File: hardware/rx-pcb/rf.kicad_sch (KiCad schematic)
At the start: 1 part

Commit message: minor board updates. added the MLPF-WB chip for stm impedance matching
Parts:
- removed FL1: MLPF-WB-01D3, easyeda2kicad:BGA-6_L1.6-W1.0-R3-C2-P0.50-TL, symbol easyeda2kicad:MLPF-WB-01D3
- added FL1: MLPF-WB-01D3, easyeda:BGA-6_L1.6-W1.0-R3-C2-P0.50-TL, symbol easyeda:MLPF-WB-01D3
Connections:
- net GND: now also FL1.A2 (GND4), FL1.B1 (GND3), FL1.B2 (GND2), FL1.B3 (GND1)
- net RF1: now also FL1.A3 (IN)
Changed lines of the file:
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@@
 		(instances
 			(project "rx-pcb"
-				(path "/9df8ddb8-545e-44cf-b4e7-941b19ec42ab/84ed0e1d-ea4c-4524-b4ef-48cf817ee110"
-					(reference "#PWR017")
-					(unit 1)
-				)
 				(path "/9df8ddb8-545e-44cf-b4e7-941b19ec42ab/f451fa07-6b2e-4005-ab57-ecfade312cca"
 					(reference "#PWR016")
@@
 	)
 	(symbol
-		(lib_id "easyeda2kicad:MLPF-WB-01D3")
+		(lib_id "easyeda:MLPF-WB-01D3")
 		(at 48.26 62.23 270)
 		(unit 1)
@@
 			)
 		)
-		(property "Footprint" "easyeda2kicad:BGA-6_L1.6-W1.0-R3-C2-P0.50-TL"
+		(property "Footprint" "easyeda:BGA-6_L1.6-W1.0-R3-C2-P0.50-TL"
 			(at 38.1 62.23 0)
 			(effects
@@
 			)
 		)
-		(property "Datasheet" ""
-			(at 48.26 62.23 0)
+		(property "Datasheet" "https://www.lcsc.com/datasheet/C5440144.pdf"
+			(at 35.56 62.23 0)
 			(effects
 				(font
@@
 			)
 		)
+		(property "Manufacturer" "ST(意法半导体)"
+			(at 33.02 62.23 0)
+			(effects
+				(font
+					(size 1.27 1.27)
+				)
+				(hide yes)
+			)
+		)
+		(property "MPN" "MLPF-WB-01D3"
+			(at 30.48 62.23 0)
+			(effects
+				(font
+					(size 1.27 1.27)
+				)
+				(hide yes)
+			)
+		)
 		(property "LCSC Part" "C5440144"
-			(at 35.56 62.23 0)
+			(at 27.94 62.23 0)
 			(effects
 				(font
@@
 		(pin "A1"
 		)
-		(pin "A2"
+		(pin "B2"
 		)
 		(pin "B1"
 		)
-		(pin "B2"
-		)
 		(pin "B3"
 		)
+		(pin "A2"
+		)
 		(instances
-			(project ""
-				(path "/9df8ddb8-545e-44cf-b4e7-941b19ec42ab/84ed0e1d-ea4c-4524-b4ef-48cf817ee110"
-					(reference "FL2")
-					(unit 1)
-				)
+			(project "rx-pcb"
 				(path "/9df8ddb8-545e-44cf-b4e7-941b19ec42ab/f451fa07-6b2e-4005-ab57-ecfade312cca"
 					(reference "FL1")
@@
 		)
 		(instances
-			(project ""
-				(path "/9df8ddb8-545e-44cf-b4e7-941b19ec42ab/84ed0e1d-ea4c-4524-b4ef-48cf817ee110"
-					(reference "#PWR015")
-					(unit 1)
-				)
+			(project "rx-pcb"
 				(path "/9df8ddb8-545e-44cf-b4e7-941b19ec42ab/f451fa07-6b2e-4005-ab57-ecfade312cca"
 					(reference "#PWR06")

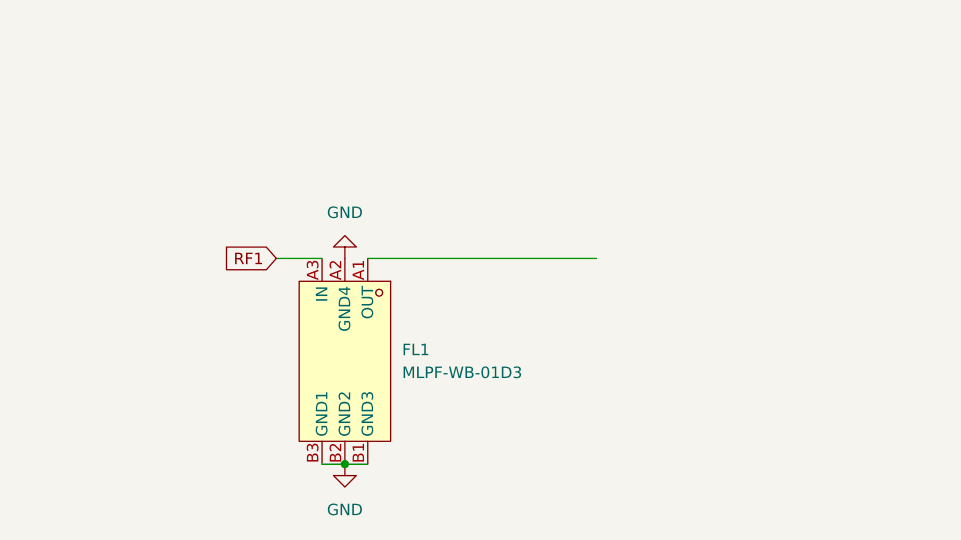
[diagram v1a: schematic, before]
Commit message: finished initial board. no sensors or power harvesting, but its programmable and bluetooth should work.
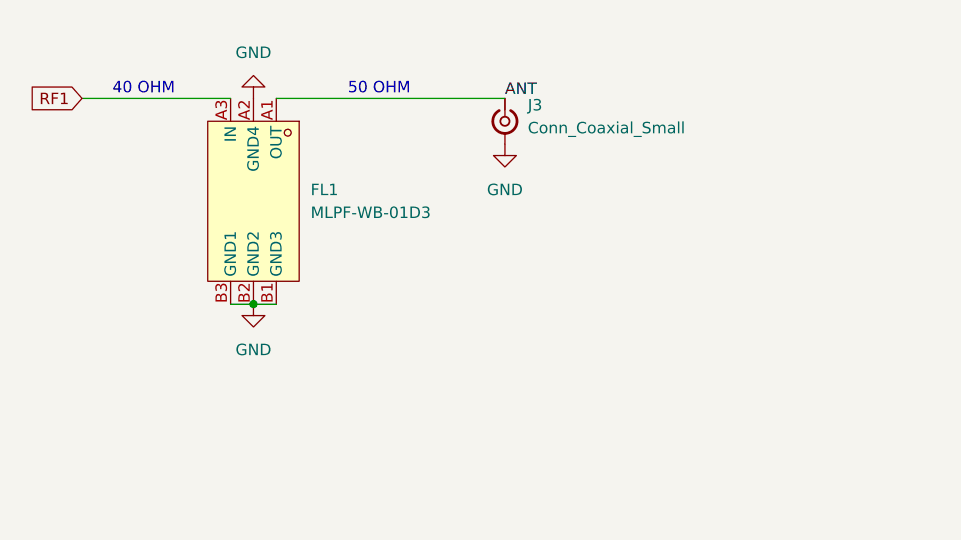
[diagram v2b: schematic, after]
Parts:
- removed FL1: MLPF-WB-01D3, easyeda:BGA-6_L1.6-W1.0-R3-C2-P0.50-TL, symbol easyeda:MLPF-WB-01D3
- added FL1: MLPF-WB-01D3, rx-parts:BGA-6_L1.6-W1.0-R3-C2-P0.50-TL, symbol rx-parts:MLPF-WB-01D3
- added J3: Conn_Coaxial_Small, rx-parts:SMA_Amphenol_901-143_Horizontal, symbol rx-parts:Conn_Coaxial_Small
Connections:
- net GND: now also FL1.A2 (GND4), FL1.B1 (GND3), FL1.B2 (GND2), FL1.B3 (GND1), J3.2 (Ext)
- net RF1: now also FL1.A3 (IN)
- new net ANT: FL1.A1 (OUT), J3.1 (In)
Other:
- note added: "40 OHM"
- note added: "50 OHM"
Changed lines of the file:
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@@
 	(generator_version "9.0")
 	(paper "A4")
+	(text "40 OHM"
+		(exclude_from_sim no)
+		(at 25.908 32.004 0)
+		(effects
+			(font
+				(size 1.27 1.27)
+			)
+		)
+	)
+	(text "50 OHM"
+		(exclude_from_sim no)
+		(at 52.07 32.004 0)
+		(effects
+			(font
+				(size 1.27 1.27)
+			)
+		)
+	)
 	(junction
-		(at 48.26 73.66)
+		(at 38.1 55.88)
 		(diameter 0)
 		(color 0 0 0 0)
@@
 	(wire
 		(pts
-			(xy 45.72 73.66) (xy 48.26 73.66)
+			(xy 35.56 55.88) (xy 38.1 55.88)
 		)
 		(stroke
@@
 	(wire
 		(pts
-			(xy 40.64 50.8) (xy 45.72 50.8)
+			(xy 19.05 33.02) (xy 35.56 33.02)
 		)
 		(stroke
@@
 	(wire
 		(pts
-			(xy 50.8 50.8) (xy 76.2 50.8)
+			(xy 40.64 33.02) (xy 66.04 33.02)
 		)
 		(stroke
@@
 	(wire
 		(pts
-			(xy 48.26 73.66) (xy 50.8 73.66)
+			(xy 38.1 55.88) (xy 40.64 55.88)
 		)
 		(stroke
@@
 		)
 	)
-	(global_label "RF1"
-		(shape input)
-		(at 40.64 50.8 180)
-		(fields_autoplaced yes)
+	(label "ANT"
+		(at 66.04 33.02 0)
 		(effects
 			(font
 				(size 1.27 1.27)
 			)
+			(justify left bottom)
+		)
+	)
+	(global_label "RF1"
+		(shape input)
+		(at 19.05 33.02 180)
+		(fields_autoplaced yes)
+		(effects
+			(font
+				(size 1.27 1.27)
+			)
 			(justify right)
 		)
 		(property "Intersheetrefs" "${INTERSHEET_REFS}"
-			(at 34.0867 50.8 0)
+			(at 12.4967 33.02 0)
 			(effects
 				(font
@@
 	)
 	(symbol
-		(lib_id "power:GND")
-		(at 48.26 73.66 0)
+		(lib_id "rx-parts:GND")
+		(at 38.1 55.88 0)
 		(unit 1)
 		(exclude_from_sim no)
@@
 		(fields_autoplaced yes)
 		(property "Reference" "#PWR016"
-			(at 48.26 80.01 0)
+			(at 38.1 62.23 0)
 			(effects
 				(font
@@
 		)
 		(property "Value" "GND"
-			(at 48.26 78.74 0)
+			(at 38.1 60.96 0)
 			(effects
 				(font
@@
 		)
 		(property "Footprint" ""
-			(at 48.26 73.66 0)
+			(at 38.1 55.88 0)
 			(effects
 				(font
@@
 		)
 		(property "Datasheet" ""
-			(at 48.26 73.66 0)
+			(at 38.1 55.88 0)
 			(effects
 				(font
@@
 		)
 		(property "Description" "Power symbol creates a global label with name \"GND\" , ground"
-			(at 48.26 73.66 0)
+			(at 38.1 55.88 0)
 			(effects
 				(font
@@
 	)
 	(symbol
-		(lib_id "easyeda:MLPF-WB-01D3")
-		(at 48.26 62.23 270)
+		(lib_id "rx-parts:MLPF-WB-01D3")
+		(at 38.1 44.45 270)
 		(unit 1)
 		(exclude_from_sim no)
@@
 		(fields_autoplaced yes)
 		(property "Reference" "FL1"
-			(at 54.61 60.9599 90)
+			(at 44.45 43.1799 90)
 			(effects
 				(font
@@
 		)
 		(property "Value" "MLPF-WB-01D3"
-			(at 54.61 63.4999 90)
+			(at 44.45 45.7199 90)
 			(effects
 				(font
@@
 			)
 		)
-		(property "Footprint" "easyeda:BGA-6_L1.6-W1.0-R3-C2-P0.50-TL"
-			(at 38.1 62.23 0)
+		(property "Footprint" "rx-parts:BGA-6_L1.6-W1.0-R3-C2-P0.50-TL"
+			(at 27.94 44.45 0)
 			(effects
 				(font
@@
 		)
 		(property "Datasheet" "https://www.lcsc.com/datasheet/C5440144.pdf"
-			(at 35.56 62.23 0)
+			(at 25.4 44.45 0)
 			(effects
 				(font
@@
 		)
 		(property "Description" ""
-			(at 48.26 62.23 0)
+			(at 38.1 44.45 0)
 			(effects
 				(font
@@
 		)
 		(property "Manufacturer" "ST(意法半导体)"
-			(at 33.02 62.23 0)
+			(at 22.86 44.45 0)
 			(effects
 				(font
@@
 		)
 		(property "MPN" "MLPF-WB-01D3"
-			(at 30.48 62.23 0)
+			(at 20.32 44.45 0)
 			(effects
 				(font
@@
 		)
 		(property "LCSC Part" "C5440144"
-			(at 27.94 62.23 0)
-			(effects
-				(font
-					(size 1.27 1.27)
-				)
-				(hide yes)
-			)
+			(at 17.78 44.45 0)
+			(effects
+				(font
+					(size 1.27 1.27)
+				)
+				(hide yes)
+			)
+		)
+		(pin "A1"
+		)
+		(pin "A2"
+		)
+		(pin "B1"
+		)
+		(pin "B2"
 		)
 		(pin "A3"
 		)
-		(pin "A1"
-		)
-		(pin "B2"
-		)
-		(pin "B1"
-		)
 		(pin "B3"
 		)
-		(pin "A2"
+	)
+	(symbol
+		(lib_id "rx-parts:Conn_Coaxial_Small")
+		(at 66.04 35.56 270)
+		(unit 1)
+		(exclude_from_sim no)
+		(in_bom yes)
+		(on_board yes)
+		(dnp no)
+		(fields_autoplaced yes)
+		(property "Reference" "J3"
+			(at 68.58 33.7703 90)
+			(effects
+				(font
+					(size 1.27 1.27)
+				)
+				(justify left)
+			)
+		)
+		(property "Value" "Conn_Coaxial_Small"
+			(at 68.58 36.3103 90)
+			(effects
+				(font
+					(size 1.27 1.27)
+				)
+				(justify left)
+			)
+		)
+		(property "Footprint" "rx-parts:SMA_Amphenol_901-143_Horizontal"
+			(at 66.04 35.56 0)
+			(effects
+				(font
+					(size 1.27 1.27)
+				)
+				(hide yes)
+			)
+		)
+		(property "Datasheet" "~"
+			(at 66.04 35.56 0)
+			(effects
+				(font
+					(size 1.27 1.27)
+				)
+				(hide yes)
+			)
+		)
+		(property "Description" "small coaxial connector (BNC, SMA, SMB, SMC, Cinch/RCA, LEMO, ...)"
+			(at 66.04 35.56 0)
+			(effects
+				(font
+					(size 1.27 1.27)
+				)
+				(hide yes)
+			)
+		)
+		(pin "2"
+		)
+		(pin "1"
+		)
+	)
+	(symbol
+		(lib_id "rx-parts:GND")
+		(at 66.04 38.1 0)
+		(unit 1)
+		(exclude_from_sim no)
+		(in_bom yes)
+		(on_board yes)
+		(dnp no)
+		(fields_autoplaced yes)
+		(property "Reference" "#PWR015"
+			(at 66.04 44.45 0)
+			(effects
+				(font
+					(size 1.27 1.27)
+				)
+				(hide yes)
+			)
+		)
+		(property "Value" "GND"
+			(at 66.04 43.18 0)
+			(effects
+				(font
+					(size 1.27 1.27)
+				)
+			)
+		)
+		(property "Footprint" ""
+			(at 66.04 38.1 0)
+			(effects
+				(font
+					(size 1.27 1.27)
+				)
+				(hide yes)
+			)
+		)
+		(property "Datasheet" ""
+			(at 66.04 38.1 0)
+			(effects
+				(font
+					(size 1.27 1.27)
+				)
+				(hide yes)
+			)
+		)
+		(property "Description" "Power symbol creates a global label with name \"GND\" , ground"
+			(at 66.04 38.1 0)
+			(effects
+				(font
+					(size 1.27 1.27)
+				)
+				(hide yes)
+			)
+		)
+		(pin "1"
 		)
 		(instances
 			(project "rx-pcb"
 				(path "/9df8ddb8-545e-44cf-b4e7-941b19ec42ab/f451fa07-6b2e-4005-ab57-ecfade312cca"
-					(reference "FL1")
+					(reference "#PWR015")
 					(unit 1)
 				)
@@
 	)
 	(symbol
-		(lib_id "power:GND")
-		(at 48.26 50.8 180)
+		(lib_id "rx-parts:GND")
+		(at 38.1 33.02 180)
 		(unit 1)
 		(exclude_from_sim no)
@@
 		(fields_autoplaced yes)
 		(property "Reference" "#PWR06"
-			(at 48.26 44.45 0)
+			(at 38.1 26.67 0)
 			(effects
 				(font
@@
 		)
 		(property "Value" "GND"
-			(at 48.26 45.72 0)
+			(at 38.1 27.94 0)
 			(effects
 				(font
@@
 		)
 		(property "Footprint" ""
-			(at 48.26 50.8 0)
+			(at 38.1 33.02 0)
 			(effects
 				(font
@@
 		)
 		(property "Datasheet" ""
-			(at 48.26 50.8 0)
+			(at 38.1 33.02 0)
 			(effects
 				(font
@@
 		)
 		(property "Description" "Power symbol creates a global label with name \"GND\" , ground"
-			(at 48.26 50.8 0)
-			(effects
-				(font
+			(at 38.1 33.02 0)
+			(effects
+				(font

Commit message: updated bluetooth section to be in-line with filter datasheet. rearranged LFEX to allow I2C connection.
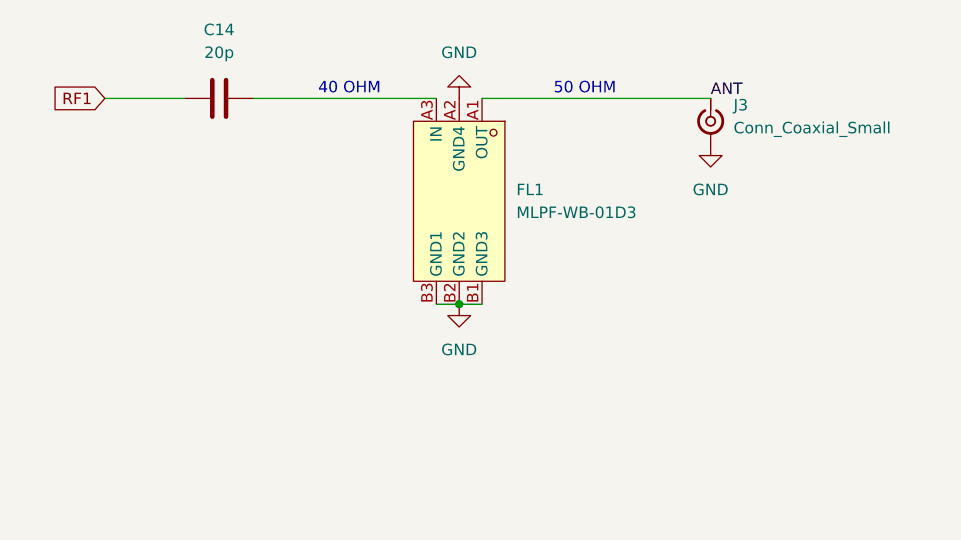
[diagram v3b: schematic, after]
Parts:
- added C14: 20p, Capacitor_SMD:C_0201_0603Metric_Pad0.64x0.40mm_HandSolder, symbol Device:C
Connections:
- net RF1: now also C14.1; no longer FL1.A3 (IN)
- new net: C14.2, FL1.A3 (IN)
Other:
- moved on the sheet: FL1, J3
